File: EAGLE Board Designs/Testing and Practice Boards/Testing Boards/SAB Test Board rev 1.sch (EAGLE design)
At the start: 103 parts, among them J1 CONNECTOR-4_μF_S_RA_, J2 CONNECTOR-8_μF_T_V_BLACK, J3 CONNECTOR-4_μF_T_V_BLACK, J4 CONNECTOR-6_μF_T_V_BLACK, J5 CONNECTOR-2_μF_T_V_BLACK, U1 TPS54202DDCR, U10 MCP2515, U2 MCP2551, U6 OPAMP_1_CHANNEL_OPA991, U7 MAX3075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

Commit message: Adjusted connector and protection circuit
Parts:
- removed J5: CONNECTOR-2_μF_T_V_BLACK, HyTechDevices:CONNECTOR-2_μF_T_V_BLACK
- added J6: CONNECTOR-4_μF_T_V_BLACK, HyTechDevices:CONNECTOR-4_μF_T_V_BLACK
- added JP3, JP5, JP6: JUMPER__1X02, HyTechDevices:JUMPER__1X02
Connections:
- removed net N$40: U$3.A
- new net 5VIN: J6.1, U$3.A
- new net N$41: C22.1, C23.1, C24.1, JP3.1, L1.2, R35.2
- new net N$42: C7.1, JP5.1, JP6.1, U9G$2.VDD
- net +3V3: now also A1.3.3V, JP3.2, JP6.2; no longer C22.1, C23.1, C24.1, L1.2, R35.2
- net GND: now also J6.4
- net LTCIN: now also J6.2; no longer J5.1
- net LTCOUT: now also J6.3; no longer J5.2
- net P7: now also JP5.2; no longer C7.1, U9G$2.VDD
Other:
- moved on the sheet: C14, C19, C20, C27, C4, J4, R38, R39, R40, R41, R42, R43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

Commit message: Changes made
Changes made to SAB
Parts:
- removed C16: CAPACITOR_0603_10V_0.1UF, HyTechDevices:CAPACITOR_0603_10V_0.1UF
- removed R18: RESISTOR_0603_0, HyTechDevices:RESISTOR_0603_0
- removed TP13, TP14: TEST_POINT, HyTechDevices:TEST_POINT
- added C5: CAPACITOR_0603_10V_1UF, HyTechDevices:CAPACITOR_0603_10V_1UF
- added JP7: JUMPER__1X02, HyTechDevices:JUMPER__1X02
- added R4: RESISTOR_0603_3.32K, HyTechDevices:RESISTOR_0603_3.32K
- J1: value CONNECTOR-4_μF_S_RA_ -> CONNECTOR-4_μF_T_V_BLACK; device HyTechDevices:CONNECTOR-4_μF_S_RA_ -> HyTechDevices:CONNECTOR-4_μF_T_V_BLACK
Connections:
- removed net N$10: R30.2
- removed net N$14: TP13.1
- removed net N$15: TP14.1
- removed net N$16: TP15.1
- removed net N$24: R28.2
- removed net N$26: R24.2
- removed net N$31: R22.1, U6A.VOUT
- removed net N$36: R25.1
- removed net N$37: R23.2
- removed net N$38: R32.1
- removed net N$39: C12.1
- removed net N$6: R31.2
- new net FIRST_ORDER_FILT: A1.A2, JP7.2
- net +5V: now also C5.1; no longer C16.1
- net GND: now also C5.2; no longer C16.2
- net N$12: now also R32.1
- net N$19: now also C12.1
- net N$21: now also R4.2; no longer R18.2
- net N$22: now also R4.1; no longer R18.1
- net N$28: now also R30.2, R31.2
- net N$9: now also R22.1, R25.1, R28.2, U6A.VOUT
- net P3: now also R23.2, R24.2, TP15.1
- net P9: now also JP7.1
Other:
- moved on the sheet: R19, TP15

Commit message: Board Test
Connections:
- net FIRST_ORDER_FILT renamed FOURTH_ORDER_FILT
- net +3V3: now also C19.1, C20.1
- net +5V: no longer C19.1, C20.1
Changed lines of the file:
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@@
-</segment>
-<segment>
-<pinref part="C19" gate="G$1" pin="2"/>
-<wire x1="254" y1="172.72" x2="254" y2="170.18" width="0.1524" layer="91"/>
-<pinref part="P49" gate="1" pin="GND"/>
-<wire x1="254" y1="170.18" x2="264.16" y2="170.18" width="0.1524" layer="91"/>
-<pinref part="C20" gate="G$1" pin="2"/>
-<wire x1="264.16" y1="172.72" x2="264.16" y2="170.18" width="0.1524" layer="91"/>
-<junction x="264.16" y="170.18"/>
 </segment>
 <segment>
@@
 <wire x1="175.26" y1="195.58" x2="175.26" y2="193.04" width="0.1524" layer="91"/>
 </segment>
+<segment>
+<pinref part="C19" gate="G$1" pin="2"/>
+<wire x1="254" y1="172.72" x2="254" y2="170.18" width="0.1524" layer="91"/>
+<pinref part="P49" gate="1" pin="GND"/>
+<wire x1="254" y1="170.18" x2="264.16" y2="170.18" width="0.1524" layer="91"/>
+<pinref part="C20" gate="G$1" pin="2"/>
+<wire x1="264.16" y1="172.72" x2="264.16" y2="170.18" width="0.1524" layer="91"/>
+<junction x="264.16" y="170.18"/>
+</segment>
 </net>
 <net name="TXCAN" class="0">
@@
 </segment>
 <segment>
-<pinref part="P48" gate="G$1" pin="+3V3"/>
-<pinref part="C19" gate="G$1" pin="1"/>
-<wire x1="254" y1="185.42" x2="254" y2="180.34" width="0.1524" layer="91"/>
-<pinref part="C20" gate="G$1" pin="1"/>
-<wire x1="254" y1="180.34" x2="264.16" y2="180.34" width="0.1524" layer="91"/>
-<junction x="254" y="180.34"/>
-</segment>
-<segment>
 <pinref part="U2" gate="G$1" pin="VDD"/>
 <wire x1="53.34" y1="119.38" x2="55.88" y2="119.38" width="0.1524" layer="91"/>
@@
 <wire x1="43.18" y1="180.34" x2="53.34" y2="180.34" width="0.1524" layer="91"/>
 <wire x1="53.34" y1="180.34" x2="53.34" y2="182.88" width="0.1524" layer="91"/>
+</segment>
+<segment>
+<pinref part="P48" gate="G$1" pin="+3V3"/>
+<pinref part="C19" gate="G$1" pin="1"/>
+<wire x1="254" y1="185.42" x2="254" y2="180.34" width="0.1524" layer="91"/>
+<pinref part="C20" gate="G$1" pin="1"/>
+<wire x1="264.16" y1="180.34" x2="254" y2="180.34" width="0.1524" layer="91"/>
+<junction x="254" y="180.34"/>
 </segment>
 </net>
@@
 </segment>
 </net>
-<net name="FIRST_ORDER_FILT" class="0">
+<net name="FOURTH_ORDER_FILT" class="0">
 <segment>
 <pinref part="A1" gate="G$1" pin="A2"/>
@@
 </segment>
 </net>
-<net name="FIRST_ORDER_FILT" class="0">
+<net name="FOURTH_ORDER_FILT" class="0">
 <segment>
 <pinref part="JP7" gate="G$1" pin="2"/>

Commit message: Board changes
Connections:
- removed net +5V1: C13.1, C26.1, U7.VCC
- net +3V3: now also C13.1, C26.1, U7.VCC
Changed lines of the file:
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@@
-</segment>
-<segment>
-<pinref part="C13" gate="G$1" pin="2"/>
-<wire x1="129.54" y1="154.94" x2="127" y2="154.94" width="0.1524" layer="91"/>
-<pinref part="P37" gate="1" pin="GND"/>
-<pinref part="C26" gate="G$1" pin="2"/>
-<wire x1="139.7" y1="154.94" x2="129.54" y2="154.94" width="0.1524" layer="91"/>
-<junction x="129.54" y="154.94"/>
 </segment>
 <segment>
@@
 <junction x="264.16" y="170.18"/>
 </segment>
+<segment>
+<pinref part="C13" gate="G$1" pin="2"/>
+<pinref part="P37" gate="1" pin="GND"/>
+<wire x1="129.54" y1="154.94" x2="127" y2="154.94" width="0.1524" layer="91"/>
+<pinref part="C26" gate="G$1" pin="2"/>
+<wire x1="129.54" y1="154.94" x2="139.7" y2="154.94" width="0.1524" layer="91"/>
+<junction x="129.54" y="154.94"/>
+</segment>
 </net>
 <net name="TXCAN" class="0">
@@
 <wire x1="264.16" y1="180.34" x2="254" y2="180.34" width="0.1524" layer="91"/>
 <junction x="254" y="180.34"/>
+</segment>
+<segment>
+<pinref part="U7" gate="G$1" pin="VCC"/>
+<wire x1="111.76" y1="167.64" x2="129.54" y2="167.64" width="0.1524" layer="91"/>
+<pinref part="P36" gate="G$1" pin="+3V3"/>
+<wire x1="129.54" y1="170.18" x2="129.54" y2="167.64" width="0.1524" layer="91"/>
+<pinref part="C13" gate="G$1" pin="1"/>
+<wire x1="129.54" y1="167.64" x2="129.54" y2="162.56" width="0.1524" layer="91"/>
+<junction x="129.54" y="167.64"/>
+<pinref part="C26" gate="G$1" pin="1"/>
+<wire x1="129.54" y1="167.64" x2="139.7" y2="167.64" width="0.1524" layer="91"/>
+<wire x1="139.7" y1="167.64" x2="139.7" y2="162.56" width="0.1524" layer="91"/>
 </segment>
 </net>
@@
 </segment>
 </net>
-<net name="+5V1" class="0">
-<segment>
-<pinref part="C13" gate="G$1" pin="1"/>
-<pinref part="U7" gate="G$1" pin="VCC"/>
-<wire x1="111.76" y1="167.64" x2="129.54" y2="167.64" width="0.1524" layer="91"/>
-<wire x1="129.54" y1="167.64" x2="129.54" y2="170.18" width="0.1524" layer="91"/>
-<pinref part="P36" gate="G$1" pin="+3V3"/>
-<wire x1="129.54" y1="167.64" x2="129.54" y2="162.56" width="0.1524" layer="91"/>
-<junction x="129.54" y="167.64"/>
-<pinref part="C26" gate="G$1" pin="1"/>
-<wire x1="139.7" y1="162.56" x2="139.7" y2="167.64" width="0.1524" layer="91"/>
-<wire x1="139.7" y1="167.64" x2="129.54" y2="167.64" width="0.1524" layer="91"/>
-</segment>
-</net>
-<net name="N$17" class="0">
-<segment>
-<pinref part="U$3" gate="G$1" pin="C"/>
-<pinref part="XF1" gate="G$1" pin="1"/>
-<wire x1="215.9" y1="195.58" x2="220.98" y2="195.58" width="0.1524" layer="91"/>
-</segment>
-</net>
 <net name="N$23" class="0">
 <segment>
@@
 </segment>
 </net>
+<net name="N$6" class="0">
+<segment>
+<pinref part="U$3" gate="G$1" pin="C"/>
+<pinref part="XF1" gate="G$1" pin="1"/>
+<wire x1="215.9" y1="195.58" x2="220.98" y2="195.58" width="0.1524" layer="91"/>
+</segment>
+</net>

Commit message: replaced diode
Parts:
- removed U$3: DIODE_SHOTTKY, HyTechSymbols:DIODE_SHOTTKY
- added D5: SCHOTTKY_1206_40V, HyTechDevices:SCHOTTKY_1206_40V
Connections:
- net 5VIN: now also D5.A; no longer U$3.A
- net N$6: now also D5.C; no longer U$3.C
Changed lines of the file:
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@@
 <part name="P38" library="HyTechSupplies" deviceset="GND" device=""/>
 <part name="XF1" library="HyTechDevices" deviceset="FUSE_HOLDER_*" device="PTH" technology="MINIBLADE"/>
-<part name="U$3" library="HyTechSymbols" deviceset="DIODE_SHOTTKY" device=""/>
 <part name="P9" library="HyTechSupplies" deviceset="+5V" device=""/>
 <part name="P8" library="HyTechSupplies" deviceset="+5V" device=""/>
@@
 <part name="C5" library="HyTechDevices" deviceset="CAPACITOR_?_*" device="0603" technology="10V_1UF"/>
 <part name="R4" library="HyTechDevices" deviceset="RESISTOR_?_*" device="0603" technology="3.32K"/>
+<part name="D5" library="HyTechDevices" deviceset="SCHOTTKY_?_*" device="1206" technology="40V"/>
 </parts>
 <sheets>
@@
 <attribute name="MPN" x="228.6" y="192.278" size="1.27" layer="96" align="top-center"/>
 </instance>
-<instance part="U$3" gate="G$1" x="213.36" y="195.58" smashed="yes">
-<attribute name="NAME" x="212.09" y="197.485" size="1.27" layer="95" align="bottom-center"/>
-</instance>
 <instance part="P9" gate="1" x="241.3" y="203.2" smashed="yes">
 <attribute name="VALUE" x="241.3" y="205.74" size="1.27" layer="96" align="bottom-center"/>
@@
 <attribute name="VOLTAGE" x="114.3" y="115.57" size="1.27" layer="96" rot="R90" align="top-center"/>
 <attribute name="CAPACITANCE" x="116.078" y="115.57" size="1.27" layer="96" rot="R90" align="top-center"/>
+</instance>
+<instance part="D5" gate="G$1" x="213.36" y="195.58" smashed="yes">
+<attribute name="NAME" x="212.09" y="197.485" size="1.27" layer="95" align="bottom-center"/>
+<attribute name="MPN" x="212.09" y="193.675" size="1.27" layer="96" align="top-center"/>
 </instance>
 </instances>
@@
 </segment>
 <segment>
-<pinref part="U$3" gate="G$1" pin="A"/>
 <wire x1="208.28" y1="195.58" x2="205.74" y2="195.58" width="0.1524" layer="91"/>
 <label x="205.74" y="195.58" size="1.27" layer="95" rot="R180" xref="yes"/>
+<pinref part="D5" gate="G$1" pin="A"/>
 </segment>
 </net>
@@
 <net name="N$6" class="0">
 <segment>
-<pinref part="U$3" gate="G$1" pin="C"/>
 <pinref part="XF1" gate="G$1" pin="1"/>
 <wire x1="215.9" y1="195.58" x2="220.98" y2="195.58" width="0.1524" layer="91"/>
-</segment>
-</net>
+<pinref part="D5" gate="G$1" pin="C"/>
+</segment>
+</net>

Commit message: Board changes
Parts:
- added JP8, JP9: JUMPER__1X02, HyTechDevices:JUMPER__1X02
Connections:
- new net N$10: JP8.1, JP9.1, U8.!LP
- net +3V3: now also JP8.2; no longer U8.!LP
- net GND: now also JP9.2
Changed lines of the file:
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@@
 <part name="R4" library="HyTechDevices" deviceset="RESISTOR_?_*" device="0603" technology="3.32K"/>
 <part name="D5" library="HyTechDevices" deviceset="SCHOTTKY_?_*" device="1206" technology="40V"/>
+<part name="JP8" library="HyTechDevices" deviceset="JUMPER_?_*" device="" technology="1X02"/>
+<part name="JP9" library="HyTechDevices" deviceset="JUMPER_?_*" device="" technology="1X02"/>
+<part name="P62" library="HyTechSupplies" deviceset="GND" device=""/>
 </parts>
 <sheets>
@@
 <attribute name="RESISTANCE" x="179.07" y="158.75" size="1.27" layer="96" rot="R90" align="top-center"/>
 </instance>
-<instance part="P59" gate="G$1" x="195.58" y="172.72" smashed="yes">
-<attribute name="VALUE" x="195.58" y="175.26" size="1.27" layer="96" align="bottom-center"/>
+<instance part="P59" gate="G$1" x="193.04" y="177.8" smashed="yes">
+<attribute name="VALUE" x="193.04" y="180.34" size="1.27" layer="96" align="bottom-center"/>
 </instance>
 <instance part="U2" gate="G$1" x="33.02" y="121.92" smashed="yes">
@@
 <attribute name="NAME" x="212.09" y="197.485" size="1.27" layer="95" align="bottom-center"/>
 <attribute name="MPN" x="212.09" y="193.675" size="1.27" layer="96" align="top-center"/>
+</instance>
+<instance part="JP8" gate="G$1" x="190.5" y="167.64" smashed="yes" rot="R90">
+<attribute name="NAME" x="187.96" y="167.64" size="1.27" layer="95" rot="R90"/>
+<attribute name="MPN" x="193.802" y="167.64" size="1.27" layer="96" rot="R90" align="top-left"/>
+</instance>
+<instance part="JP9" gate="G$1" x="195.58" y="170.18" smashed="yes" rot="R90">
+<attribute name="NAME" x="193.04" y="170.18" size="1.27" layer="95" rot="R90"/>
+<attribute name="MPN" x="198.882" y="170.18" size="1.27" layer="96" rot="R90" align="top-left"/>
+</instance>
+<instance part="P62" gate="1" x="203.2" y="172.72" smashed="yes">
+<attribute name="VALUE" x="203.2" y="171.45" size="1.27" layer="96" align="top-center"/>
 </instance>
 </instances>
@@
 <junction x="129.54" y="154.94"/>
 </segment>
+<segment>
+<pinref part="JP9" gate="G$1" pin="2"/>
+<wire x1="198.12" y1="175.26" x2="198.12" y2="177.8" width="0.1524" layer="91"/>
+<wire x1="198.12" y1="177.8" x2="203.2" y2="177.8" width="0.1524" layer="91"/>
+<wire x1="203.2" y1="177.8" x2="203.2" y2="175.26" width="0.1524" layer="91"/>
+<pinref part="P62" gate="1" pin="GND"/>
+</segment>
 </net>
 <net name="TXCAN" class="0">
@@
 <pinref part="U8" gate="G$1" pin="V+"/>
 <wire x1="231.14" y1="167.64" x2="226.06" y2="167.64" width="0.1524" layer="91"/>
-</segment>
-<segment>
-<pinref part="P59" gate="G$1" pin="+3V3"/>
-<pinref part="U8" gate="G$1" pin="!LP"/>
-<wire x1="195.58" y1="170.18" x2="195.58" y2="167.64" width="0.1524" layer="91"/>
-<wire x1="195.58" y1="167.64" x2="200.66" y2="167.64" width="0.1524" layer="91"/>
 </segment>
 <segment>
@@
 <wire x1="129.54" y1="167.64" x2="139.7" y2="167.64" width="0.1524" layer="91"/>
 <wire x1="139.7" y1="167.64" x2="139.7" y2="162.56" width="0.1524" layer="91"/>
+</segment>
+<segment>
+<pinref part="JP8" gate="G$1" pin="2"/>
+<pinref part="P59" gate="G$1" pin="+3V3"/>
+<wire x1="193.04" y1="172.72" x2="193.04" y2="175.26" width="0.1524" layer="91"/>
 </segment>
 </net>
@@
 </segment>
 </net>
+<net name="N$10" class="0">
+<segment>
+<pinref part="U8" gate="G$1" pin="!LP"/>
+<wire x1="193.04" y1="167.64" x2="198.12" y2="167.64" width="0.1524" layer="91"/>
+<pinref part="JP8" gate="G$1" pin="1"/>
+<wire x1="198.12" y1="167.64" x2="200.66" y2="167.64" width="0.1524" layer="91"/>
+<wire x1="198.12" y1="167.64" x2="198.12" y2="170.18" width="0.1524" layer="91"/>
+<junction x="198.12" y="167.64"/>
+<pinref part="JP9" gate="G$1" pin="1"/>
+</segment>
+</net>

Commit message: new board just started rev
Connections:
- net CAN_INT renamed !CAN_INT
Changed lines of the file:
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@@
 <instance part="JP8" gate="G$1" x="190.5" y="167.64" smashed="yes" rot="R90">
 <attribute name="NAME" x="187.96" y="167.64" size="1.27" layer="95" rot="R90"/>
-<attribute name="MPN" x="193.802" y="167.64" size="1.27" layer="96" rot="R90" align="top-left"/>
+<attribute name="MPN" x="183.642" y="172.72" size="1.27" layer="96" rot="R90" align="top-left"/>
 </instance>
 <instance part="JP9" gate="G$1" x="195.58" y="170.18" smashed="yes" rot="R90">
@@
 <attribute name="MPN" x="198.882" y="170.18" size="1.27" layer="96" rot="R90" align="top-left"/>
 </instance>
-<instance part="P62" gate="1" x="203.2" y="172.72" smashed="yes">
-<attribute name="VALUE" x="203.2" y="171.45" size="1.27" layer="96" align="top-center"/>
+<instance part="P62" gate="1" x="198.12" y="180.34" smashed="yes" rot="R180">
+<attribute name="VALUE" x="198.12" y="181.61" size="1.27" layer="96" rot="R180" align="top-center"/>
 </instance>
 </instances>
@@
 <pinref part="JP9" gate="G$1" pin="2"/>
 <wire x1="198.12" y1="175.26" x2="198.12" y2="177.8" width="0.1524" layer="91"/>
-<wire x1="198.12" y1="177.8" x2="203.2" y2="177.8" width="0.1524" layer="91"/>
-<wire x1="203.2" y1="177.8" x2="203.2" y2="175.26" width="0.1524" layer="91"/>
 <pinref part="P62" gate="1" pin="GND"/>
 </segment>
@@
 </segment>
 </net>
-<net name="CAN_INT" class="0">
+<net name="!CAN_INT" class="0">
 <segment>
 <wire x1="50.8" y1="15.24" x2="45.72" y2="15.24" width="0.1524" layer="91"/>

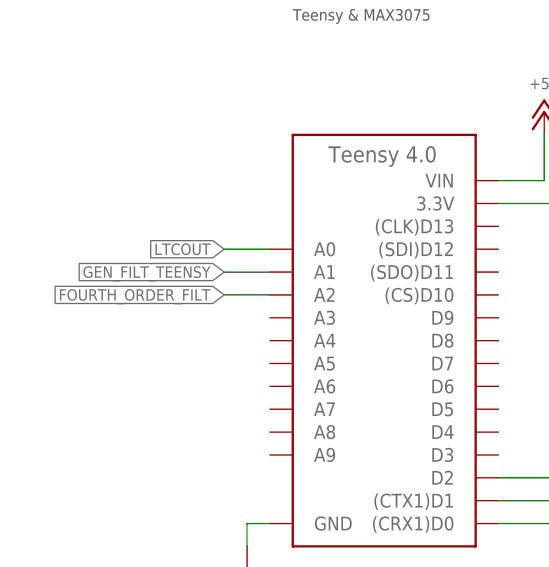
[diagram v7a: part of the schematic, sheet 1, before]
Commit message: moved analog port to be easier for routing
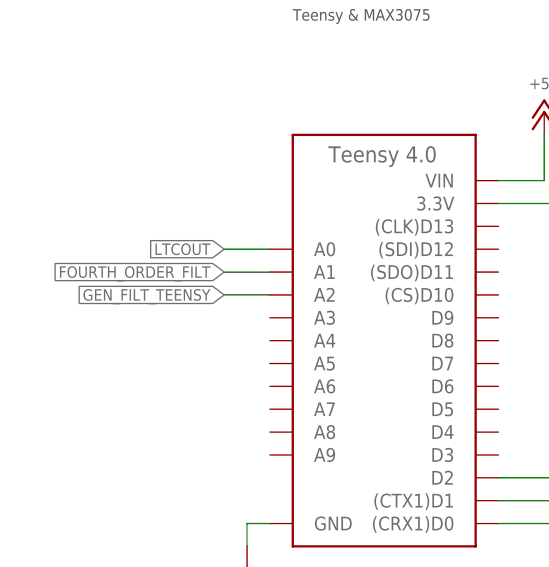
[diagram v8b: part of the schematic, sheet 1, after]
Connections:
- net FOURTH_ORDER_FILT: now also A1.A1; no longer A1.A2
- net GEN_FILT_TEENSY: now also A1.A2; no longer A1.A1
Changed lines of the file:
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@@
 </segment>
 <segment>
-<pinref part="A1" gate="G$1" pin="A1"/>
-<wire x1="17.78" y1="172.72" x2="12.7" y2="172.72" width="0.1524" layer="91"/>
-<label x="12.7" y="172.72" size="1.27" layer="95" rot="R180" xref="yes"/>
+<label x="12.7" y="170.18" size="1.27" layer="95" rot="R180" xref="yes"/>
+<wire x1="12.7" y1="170.18" x2="17.78" y2="170.18" width="0.1524" layer="91"/>
+<pinref part="A1" gate="G$1" pin="A2"/>
 </segment>
 </net>
@@
 <net name="FOURTH_ORDER_FILT" class="0">
 <segment>
-<pinref part="A1" gate="G$1" pin="A2"/>
-<wire x1="17.78" y1="170.18" x2="12.7" y2="170.18" width="0.1524" layer="91"/>
-<label x="12.7" y="170.18" size="1.27" layer="95" rot="R180" xref="yes"/>
+<label x="12.7" y="172.72" size="1.27" layer="95" rot="R180" xref="yes"/>
+<wire x1="12.7" y1="172.72" x2="17.78" y2="172.72" width="0.1524" layer="91"/>
+<pinref part="A1" gate="G$1" pin="A1"/>
 </segment>
 </net>
